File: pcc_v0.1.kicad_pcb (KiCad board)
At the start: 2 copper layers, 49 parts, among them J1 Conn_01x05_Socket, J2 Conn_01x03_Socket, J3 Conn_01x05_Socket, K2 CPC1706, Q2 BS108, U2 4N35, U3 4N35, U7 Teensy4.0, U8 SN65HVD230

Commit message: polishing layout
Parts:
- removed R28: 10K, Resistor_SMD:R_0805_2012Metric
- removed U7: Teensy4.0, Package_DIP:DIP-28_W15.24mm_Socket
- added J4: Conn_02x14_Counter_Clockwise, Package_DIP:DIP-28_W15.24mm_Socket, F.Cu at (103.8, 59.4)
- C2, C7: value 10n -> 100n
- C3, C6: value 100n -> 10n
- moved J3 117.9 mm to (87.6, 83.5)
- moved U6 81.0 mm to (175.5, 52.5)
- moved R19 80.8 mm to (188.6, 109.5)
- moved C7 75.9 mm to (180.0, 118.3), turned to -90 degrees
- moved C2 73.3 mm to (184.5, 118.2), turned to -90 degrees
- moved C6 69.9 mm to (175.0, 118.2), turned to -90 degrees
- moved U1 69.4 mm to (170.7, 87.7)
- moved U4 69.3 mm to (171.0, 104.0)
- moved R7 61.1 mm to (188.5, 94.0)
- moved R11 60.1 mm to (153.0, 74.7), turned to 180 degrees
- moved C5 58.3 mm to (155.1, 98.2), turned to 180 degrees
- moved R15 54.9 mm to (154.6, 109.2)
- moved R18 51.2 mm to (185.4, 70.0)
- moved R13 50.6 mm to (129.5, 102.7), turned to 90 degrees
- moved R14 46.2 mm to (147.5, 103.7), turned to -90 degrees
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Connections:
- C3 pad 1: Net-(U1-COMPIN) -> Net-(U1-RC)
- C6 pad 1: Net-(U4-COMPIN) -> Net-(U4-RC)
- R18 pad 2: Net-(U4-COMPIN) -> Net-(U4-RC)
- R9 pad 2: Net-(U1-COMPIN) -> Net-(U1-RC)
- U1 pad 5: Net-(U1-COMPIN) -> Net-(U1-RC)
- U4 pad 5: Net-(U4-COMPIN) -> Net-(U4-RC)
- U8 pad 1: /CANTX -> CANTX
- U8 pad 4: /CANRX -> CANRX

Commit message: cleaned up layout
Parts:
- removed J2: Conn_01x03_Socket, Connector_Molex:Molex_Micro-Fit_3.0_43650-0315_1x03_P3.00mm_Vertical
- removed J3: Conn_01x05_Socket, Connector_Molex:Molex_Micro-Fit_3.0_43045-0612_2x03_P3.00mm_Vertical
- added J5: Conn_01x06_Socket, Connector_Molex:Molex_Mini-Fit_Jr_5566-06A2_2x03_P4.20mm_Vertical, F.Cu at (140.0, 66.8)
- added J6: Conn_01x06_Socket, Connector_Molex:Molex_Mini-Fit_Jr_5566-06A2_2x03_P4.20mm_Vertical, F.Cu at (116.5, 77.3)
- J1: value Conn_01x05_Socket -> Conn_01x04_Socket; footprint Connector_Molex:Molex_Micro-Fit_3.0_43045-0612_2x03_P3.00mm_Vertical -> Connector_Molex:Molex_Mini-Fit_Jr_5566-04A2_2x02_P4.20mm_Vertical
- moved R13 63.0 mm to (177.2, 61.6)
- moved R12 51.5 mm to (180.7, 61.6)
- moved R26 46.7 mm to (189.2, 80.6), turned to 90 degrees
- moved U3 46.3 mm to (171.2, 74.9), turned to 90 degrees
- moved R8 44.0 mm to (189.2, 87.4), turned to -90 degrees
- moved R18 42.2 mm to (189.0, 112.0), turned to -90 degrees
- moved R11 40.5 mm to (189.0, 93.4), turned to -90 degrees
- moved C4 38.6 mm to (185.7, 87.4), turned to -90 degrees
- moved U2 38.2 mm to (181.7, 74.9), turned to 90 degrees
- moved R16 35.0 mm to (185.2, 93.5), turned to 90 degrees
- moved J4 34.5 mm to (129.8, 82.1)
- moved R14 33.0 mm to (171.0, 80.5), turned to 90 degrees
- moved Q2 29.9 mm to (119.7, 95.5)
- moved C8 29.1 mm to (178.0, 106.1), turned to 180 degrees
- moved R27 27.8 mm to (111.8, 62.4)
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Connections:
- J1 pad 1: GLV- -> GNDS
- J1 pad 2: PRECHG -> unconnected-(J1-Pin_2-Pad2)
- J1 pad 3: SHTDN_OUT -> Vin_TS
- J1 pad 4: CANL -> Vin_Accu
- U6 pad 4: (no net) -> unconnected-(U6-NC-Pad4)

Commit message: revised with all relay outputs
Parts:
- removed J5: Conn_01x06_Socket, Connector_Molex:Molex_Mini-Fit_Jr_5566-06A2_2x03_P4.20mm_Vertical
- added J2: Conn_01x04_Socket, Connector_Molex:Molex_Mini-Fit_Jr_5566-04A2_2x02_P4.20mm_Vertical, F.Cu at (43.6, 69.4)
- added J7: Conn_01x04_Socket, Connector_Molex:Molex_Mini-Fit_Jr_5566-04A2_2x02_P4.20mm_Vertical, F.Cu at (43.6, 82.5)
- added J8: Conn_01x04_Socket, Connector_Molex:Molex_Mini-Fit_Jr_5566-04A2_2x02_P4.20mm_Vertical, F.Cu at (33.9, 154.5)
- added K3: G7L-2A-X-L_DC12, KiCad:G7L2AXLDC12, F.Cu at (27.0, 76.6)
- added R28: HSA253R3J, footprints:RES_HSA25_TYCO_TYC, F.Cu at (-18.4, 119.6)
- added U9: LM1117T-5.0, Package_TO_SOT_THT:TO-220-3_Horizontal_TabDown, F.Cu at (51.9, 125.0)
- J6: value Conn_01x06_Socket -> Conn_01x04_Socket; footprint Connector_Molex:Molex_Mini-Fit_Jr_5566-06A2_2x03_P4.20mm_Vertical -> Connector_Molex:Molex_Mini-Fit_Jr_5566-04A2_2x02_P4.20mm_Vertical
- moved J6 68.6 mm to (79.8, 135.2), turned to 0 degrees
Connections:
- J6 pad 2: PRECHG -> GLV-
- J6 pad 3: SHTDN_OUT -> IR-_12V
- J6 pad 4: CANL -> IR-_12V
- K2 pad 1: Shutdown_in -> +12V
- K2 pad 3: SHTDN_OUT -> IR+_12V
- Q2 pad 2: AIR+ -> IR+

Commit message: looking to add discharge relay
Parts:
- removed Q2: BS108, Package_TO_SOT_THT:TO-92_Inline
- added U5: DMN63D8L-7, nmos:SOIC_63D8L-7_DIO, F.Cu at (116.8, 100.2)
- moved J2 183.4 mm to (216.0, 131.9), turned to 90 degrees
- moved R28 174.4 mm to (153.8, 91.4), turned to -90 degrees
- moved K3 155.9 mm to (181.2, 99.6), turned to 90 degrees
- moved U9 99.0 mm to (128.5, 62.3), turned to 90 degrees
- moved J8 81.1 mm to (103.5, 113.0), turned to -90 degrees
- moved J7 60.5 mm to (103.2, 72.5), turned to -90 degrees
- moved R18 57.6 mm to (208.2, 57.8), turned to 0 degrees
- moved R7 55.8 mm to (208.3, 61.2), turned to 0 degrees
- moved R19 52.8 mm to (208.8, 77.8), turned to 0 degrees
- moved R9 52.7 mm to (208.8, 74.2), turned to 0 degrees
- moved C9 50.0 mm to (147.6, 63.2)
- moved J6 48.7 mm to (103.5, 92.7), turned to -90 degrees
- moved C2 46.6 mm to (202.3, 86.8), turned to -90 degrees
- moved C8 44.6 mm to (202.3, 68.8), turned to -90 degrees
- moved C7 42.0 mm to (198.8, 86.8), turned to -90 degrees
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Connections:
- J4 pad 26: Precharge_Switch+ -> unconnected-(J4-Pin_26-Pad26)
- J4 pad 4: Precharge_Switch- -> unconnected-(J4-Pin_4-Pad4)
- R12 pad 2: Precharge_Switch+ -> +3.3V
- R13 pad 2: Precharge_Switch+ -> +3.3V
- U8 pad 3: Precharge_Switch+ -> +3.3V

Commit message: routed pcb
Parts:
- removed K3: G7L-2A-X-L_DC12, KiCad:G7L2AXLDC12
- added J3: Conn_01x04_Socket, Connector_Molex:Molex_Mini-Fit_Jr_5566-04A2_2x02_P4.20mm_Vertical, F.Cu at (101.2, 137.7)
- added J5: Conn_01x06_Socket, Connector_Molex:Molex_Mini-Fit_Jr_5566-06A2_2x03_P4.20mm_Vertical, F.Cu at (201.5, 89.8)
- added K1: G9KB-1A_DC12, precharge relay 2:G9KB1ADC12, F.Cu at (143.2, 145.5)
- added REF**: MountingHole_3.2mm_M3, MountingHole:MountingHole_3.2mm_M3, F.Cu at (96.2, 51.0)
- added REF**: MountingHole_3.2mm_M3, MountingHole:MountingHole_3.2mm_M3, F.Cu at (96.2, 152.5)
- added REF**: MountingHole_3.2mm_M3, MountingHole:MountingHole_3.2mm_M3, F.Cu at (212.5, 152.5)
- added REF**: MountingHole_3.2mm_M3, MountingHole:MountingHole_3.2mm_M3, F.Cu at (212.5, 51.0)
- R28: footprint footprints:RES_HSA25_TYCO_TYC -> precharge res:RES_HSA25_TYCO_TYC
- moved J2 134.0 mm to (101.3, 62.6), turned to -90 degrees
- moved R20 59.4 mm to (171.2, 85.2), turned to 180 degrees
- moved R5 52.7 mm to (175.2, 85.2), turned to 180 degrees
- moved R6 52.1 mm to (171.2, 90.5), turned to 180 degrees
- moved J4 49.0 mm to (110.6, 61.5)
- moved R24 47.5 mm to (179.2, 85.2), turned to 180 degrees
- moved R4 45.6 mm to (175.2, 90.5), turned to 180 degrees
- moved R23 42.5 mm to (183.1, 85.2), turned to 180 degrees
- moved C2 40.6 mm to (173.1, 58.5)
- moved R25 40.5 mm to (179.2, 90.5), turned to 180 degrees
- moved R28 40.1 mm to (193.0, 99.6)
- moved R22 37.5 mm to (187.1, 85.2), turned to 180 degrees
- moved R9 37.2 mm to (182.7, 47.8), turned to 180 degrees
- moved R3 35.7 mm to (183.2, 90.5), turned to 180 degrees
- moved R21 33.2 mm to (190.8, 85.2), turned to 180 degrees
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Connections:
- net IR-_12V renamed DISCHRG_COIL+
- J1 pad 1: GNDS -> DISCHRG_COM
- J1 pad 2: unconnected-(J1-Pin_2-Pad2) -> DISCHRG_COM
- J1 pad 3: Vin_TS -> DISCHRG_NO
- J1 pad 4: Vin_Accu -> DISCHRG_NO
- J4 pad 13: AIR+ -> IR+
- J4 pad 14: PRECHG -> unconnected-(J4-Pin_14-Pad14)
- J4 pad 26: unconnected-(J4-Pin_26-Pad26) -> +3.3V
- J7 pad 2: CANL -> unconnected-(J7-Pin_2-Pad2)
- J7 pad 3: CANH -> CANL
- J7 pad 4: unconnected-(J7-Pin_4-Pad4) -> CANH
- R21 pad 1: Vin_TS -> B+_out
- R28 pad 1: Net-(K3--_1) -> B+_out
- R28 pad 2: TS_in -> Vin_Accu
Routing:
- net GLV-: track 0.00 -> 330.2 mm
- net GNDS: track 0.00 -> 212.6 mm, vias 0 -> 2
- net +12P: track 0.00 -> 136.0 mm
- net DISCHRG_COIL+: track 0.00 -> 134.3 mm
- net +12V: track 0.00 -> 119.9 mm
- net Vin_Accu: track 0.00 -> 111.3 mm
- net B+_in: track 0.00 -> 92.2 mm
- net +3.3V: track 0.00 -> 70.2 mm, vias 0 -> 2
- net CANTX: track 0.00 -> 64.0 mm, vias 0 -> 1
- net CANRX: track 0.00 -> 61.4 mm, vias 0 -> 1
- net Net-(R4-Pad2): track 0.00 -> 51.3 mm, vias 0 -> 2
- net IR+_12V: track 0.00 -> 49.2 mm
- net IR+: track 0.00 -> 44.1 mm
- net Freq_Accumulator: track 0.00 -> 43.6 mm
- net DISCHRG_COM: track 0.00 -> 34.9 mm
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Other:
- board outline added: 130.2 x 115.5 mm
- board text added: "${REFERENCE}"
- board text added: "HIGH VOLTAGE"
- board text added: "LOW VOLTAGE"

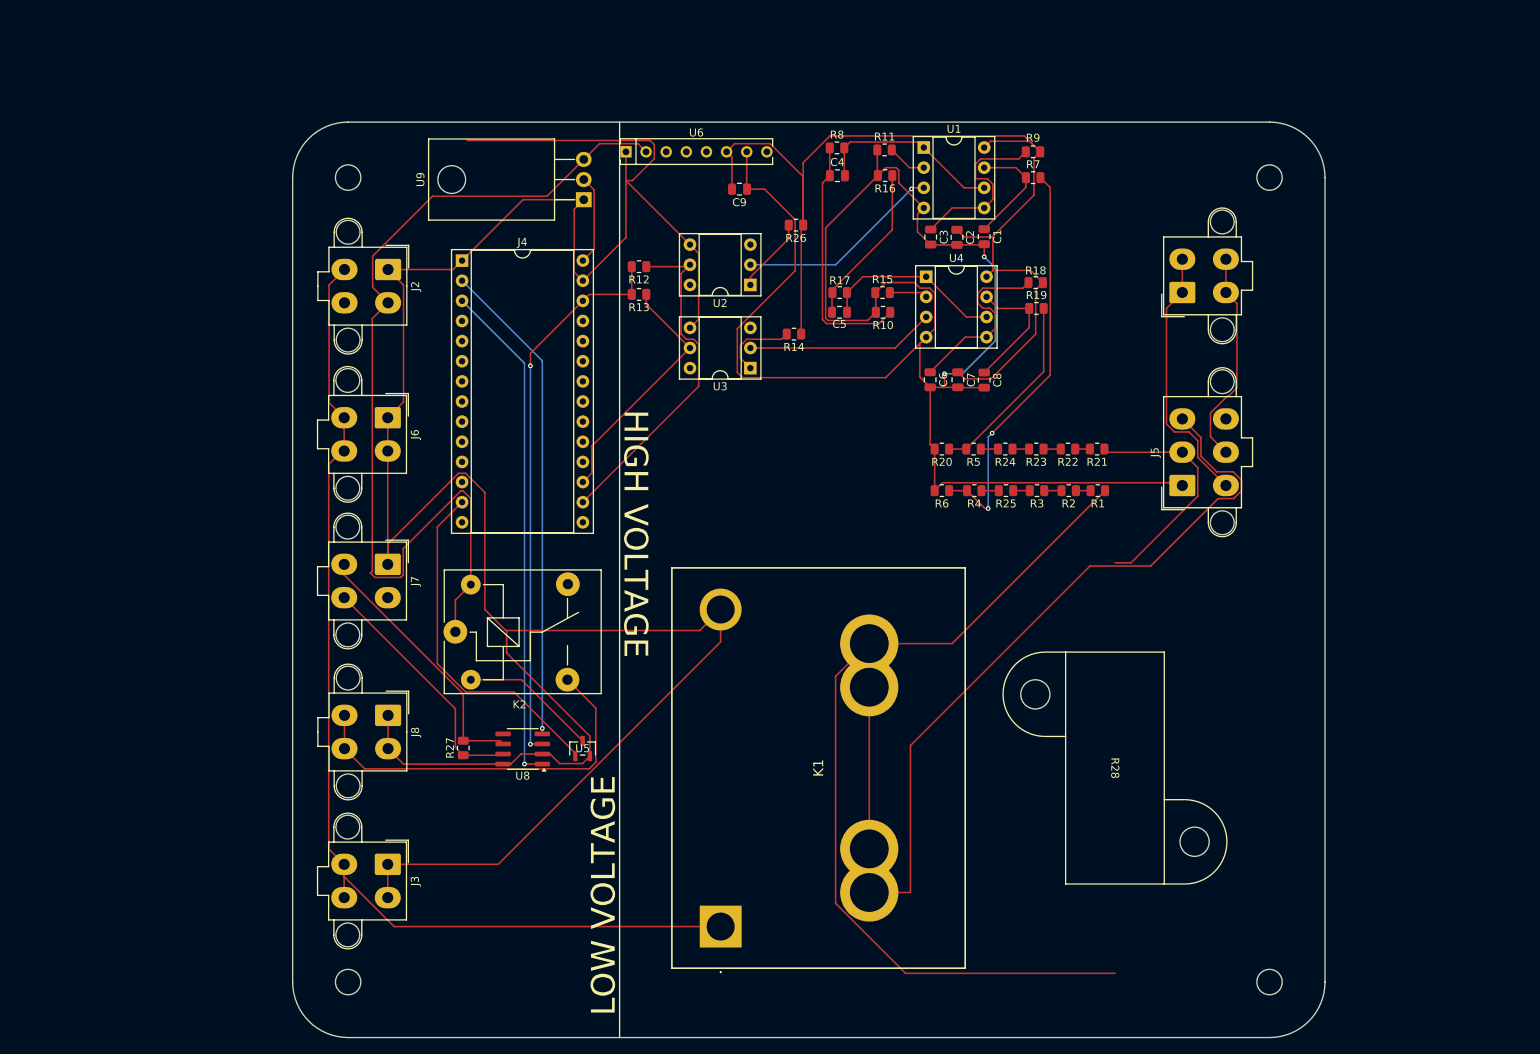
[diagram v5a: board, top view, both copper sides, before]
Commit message: next round of changes with correct precharge resistor and isolation distance
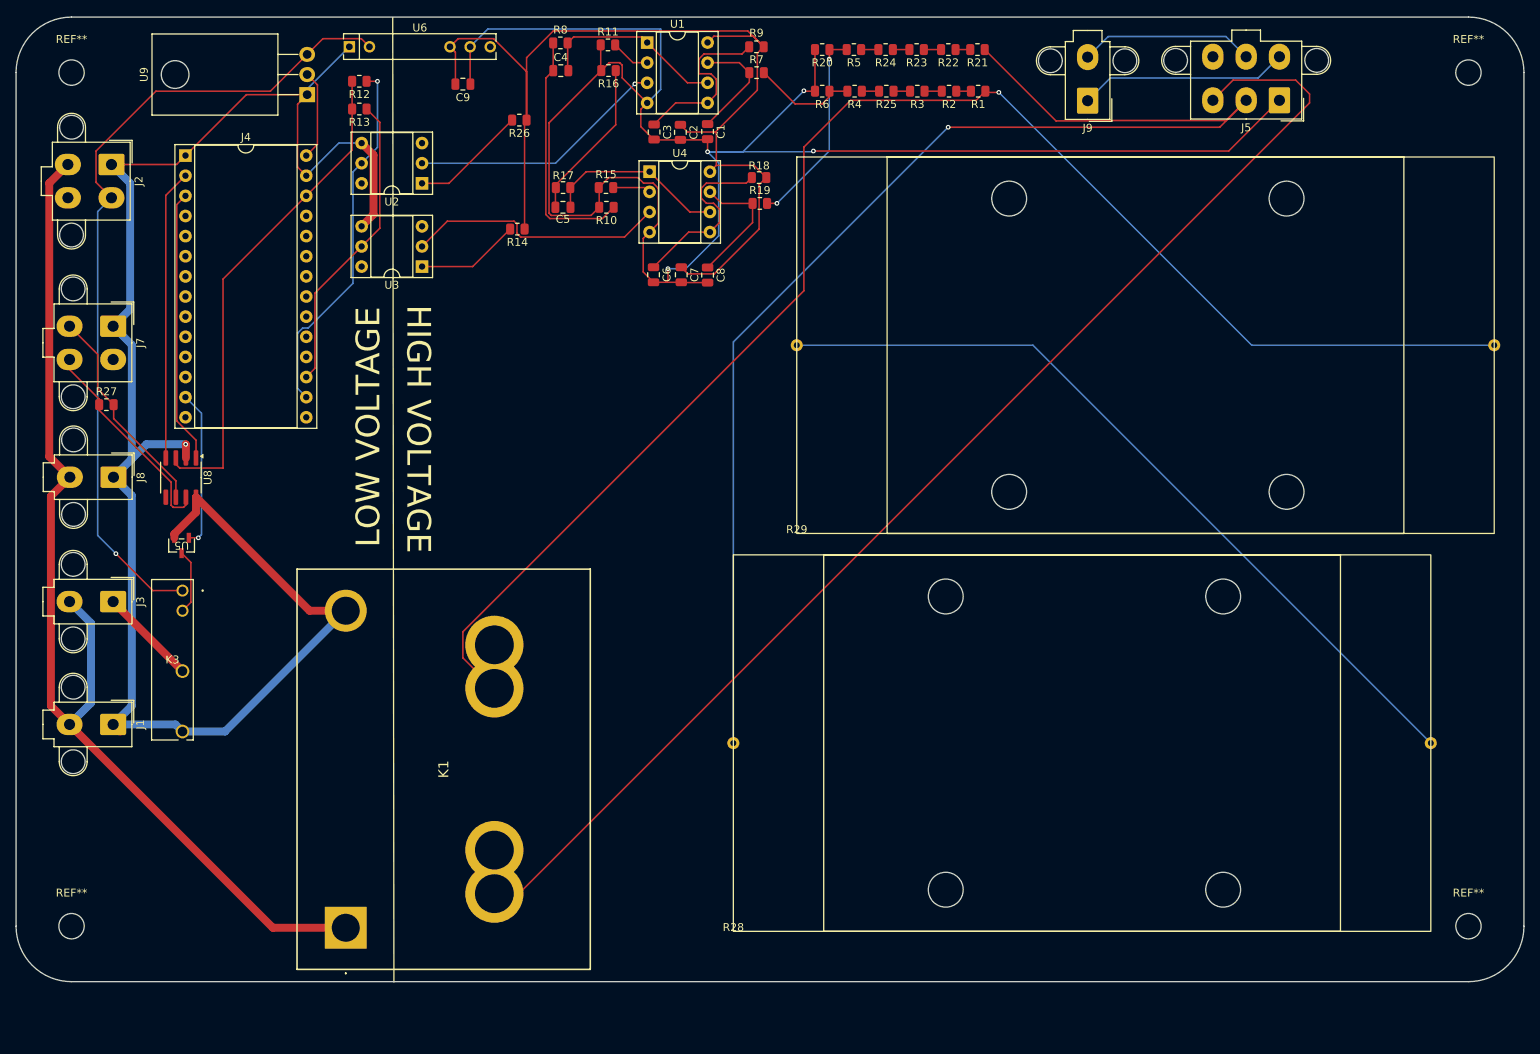
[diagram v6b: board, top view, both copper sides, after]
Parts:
- removed J6: Conn_01x04_Socket, Connector_Molex:Molex_Mini-Fit_Jr_5566-04A2_2x02_P4.20mm_Vertical
- removed K2: CPC1706, Relay_THT:Relay_SPDT_SANYOU_SRD_Series_Form_C
- removed the REF** at (96.2, 51.0)
- removed the REF** at (96.2, 152.5)
- removed the REF** at (212.5, 152.5)
- removed the REF** at (212.5, 51.0)
- added J9: Conn_01x02_Socket, Connector_Molex:Molex_Mini-Fit_Jr_5566-02A2_2x01_P4.20mm_Vertical, F.Cu at (189.6, 41.3)
- added K3: PCN-112D3MHZ_000, PCN_112D3HMZ:RELAY_PCN-105D3MHZ_000_TEC, F.Cu at (75.3, 103.1)
- added R29: 500, precharge res:Ohmite HS100 500R F, F.Cu at (152.8, 95.9)
- added REF**: MountingHole_3.2mm_M3, MountingHole:MountingHole_3.2mm_M3, F.Cu at (237.6, 145.4)
- added REF**: MountingHole_3.2mm_M3, MountingHole:MountingHole_3.2mm_M3, F.Cu at (61.4, 145.4)
- added REF**: MountingHole_3.2mm_M3, MountingHole:MountingHole_3.2mm_M3, F.Cu at (61.3, 37.7)
- added REF**: MountingHole_3.2mm_M3, MountingHole:MountingHole_3.2mm_M3, F.Cu at (237.6, 37.7)
- J1, J3, J8: value Conn_01x04_Socket -> Conn_01x02_Socket; footprint Connector_Molex:Molex_Mini-Fit_Jr_5566-04A2_2x02_P4.20mm_Vertical -> Connector_Molex:Molex_Mini-Fit_Jr_5566-02A2_2x01_P4.20mm_Vertical
- R28: value HSA253R3J -> 500; footprint precharge res:RES_HSA25_TYCO_TYC -> precharge res:Ohmite HS100 500R F
- moved J1 145.5 mm to (66.6, 120.0), turned to -90 degrees
- moved R28 66.9 mm to (144.8, 146.1), turned to 0 degrees
- moved R27 62.5 mm to (65.8, 79.7), turned to 0 degrees
- moved U5 56.7 mm to (75.2, 97.4), turned to 180 degrees
- moved U8 55.1 mm to (75.2, 88.8), turned to -90 degrees
- moved R1 52.6 mm to (175.7, 40.1)
- moved R2 52.6 mm to (172.1, 40.1)
- moved R20 52.6 mm to (156.1, 34.9)
- moved R21 52.6 mm to (175.7, 34.9)
- moved R22 52.6 mm to (172.0, 34.9)
- moved R23 52.6 mm to (168.0, 34.9)
- moved R24 52.6 mm to (164.1, 34.9)
- moved R25 52.6 mm to (164.2, 40.1)
- moved R3 52.6 mm to (168.1, 40.1)
- moved R4 52.6 mm to (160.2, 40.1)
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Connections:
- J1 pad 1: DISCHRG_COM -> GLV-
- J1 pad 2: DISCHRG_COM -> Shutdown_in
- J2 pad 3: DISCHRG_COIL+ -> Shutdown_in
- J3 pad 1: GLV- -> IR+_GND
- J3 pad 2: GLV- -> Shutdown_in
- J5 pad 4: DISCHRG_COM -> TS-
- J5 pad 5: DISCHRG_NO -> TS+
- J8 pad 2: GLV- -> Shutdown_in
- K1 pad 1: DISCHRG_COIL+ -> Shutdown_in
- K1 pad A4: Net-(K1-PadA4) -> Vin_Accu
- K1 pad B3: Net-(K1-PadA4) -> unconnected-(K1-PadB3)
- K1 pad B4: Vin_Accu -> unconnected-(K1-PadB4)
- R28 pad 2: Vin_Accu -> Net-(R28-Pad2)
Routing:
- net Shutdown_in: track 0.00 -> 137.9 mm
- net B+_out: track 30.3 -> 165.8 mm, vias 0 -> 1
- net DISCHRG_COIL+: track 134.3 -> 0.00 mm
- net GLV-: track 330.2 -> 222.2 mm, vias 0 -> 1
- net Net-(R28-Pad2): track 0.00 -> 100.8 mm
- net Vin_Accu: track 111.3 -> 191.1 mm, vias 0 -> 1
- net B+_in: track 92.2 -> 159.3 mm
- net IR+_12V: track 49.2 -> 0.00 mm
- net Net-(R4-Pad2): track 51.3 -> 13.3 mm, vias 2 -> 0
- net DISCHRG_COM: track 34.9 -> 0.00 mm
- net GNDS: track 212.6 -> 243.2 mm, vias 2 -> 4
- net CANTX: track 64.0 -> 34.5 mm, vias 1 -> 0
- net DISCHRG_NO: track 27.2 -> 0.00 mm
- net TS-: track 0.00 -> 26.5 mm
- net CANRX: track 61.4 -> 36.6 mm, vias 1 -> 0
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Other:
- board size 130.2 x 115.5 mm -> 190.3 x 121.7 mm
